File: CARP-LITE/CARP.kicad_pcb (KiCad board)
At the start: 4 copper layers, 40 x 70.1 mm, 153 parts, among them J1 USB-C, J10 PYRO_2, J11 RF_L, J3 I2C1+3V3, J4 2S XT30, J5 UART+5V+I2C1, J6 PYRO_1, J7 RF_H, J8 PWM1+5V1, J9 PWM2+5V1, Q5 SQ2318CES, Q6 SQ2318CES, Q7 SQ2318CES, SW1 SW_Push, SW2 SW_Push, U1 W25Q128JVSIMTR (16MB), U10 TPS62130A, U2 W25Q32RVXHJQ (2MB), U4 RP2350_60QFN, U5 LSM6DSO, U6 BMP390, U7 TLV75733PDBV, U9 LR2021IMLTRT, Y1 ABM8-272-T3, Y2 TG2520SMN-32.0000M-MCGNNM0

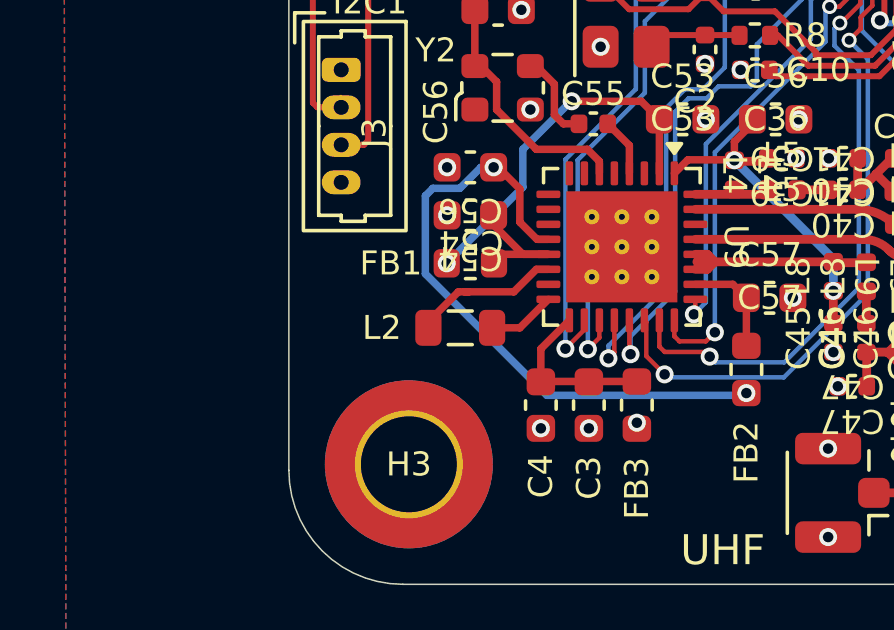
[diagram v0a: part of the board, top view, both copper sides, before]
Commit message: update inductor
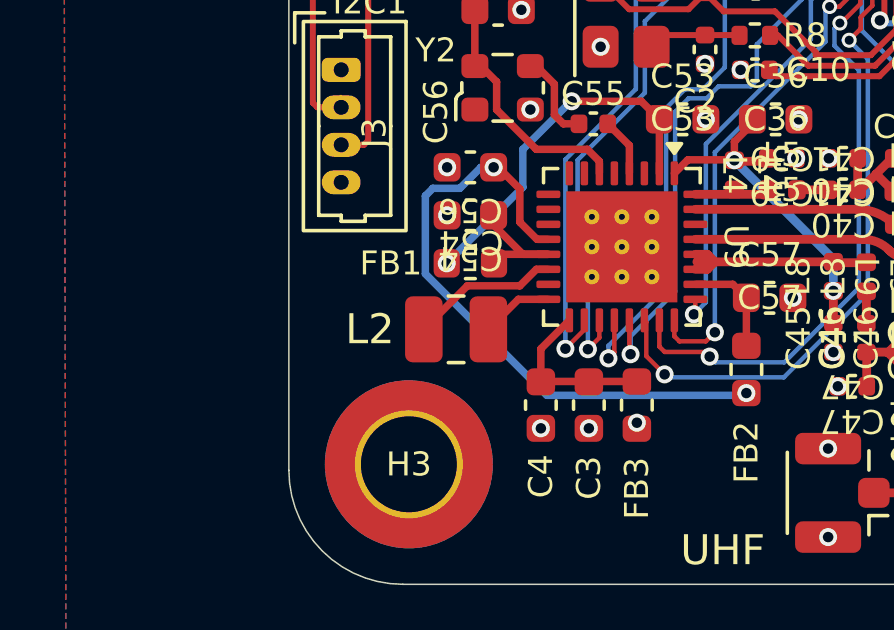
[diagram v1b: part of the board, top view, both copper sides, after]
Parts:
- L2: footprint Inductor_SMD:L_0805_2012Metric -> Inductor_SMD:L_1008_2520Metric
- moved L2 0.15 mm to (418.6, 313.3)
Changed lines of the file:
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@@
 		)
 	)
-	(footprint "Inductor_SMD:L_0805_2012Metric"
+	(footprint "Inductor_SMD:L_1008_2520Metric"
 		(layer "F.Cu")
-		(at 418.7125 313.25 180)
-		(descr "Inductor SMD 0805 (2012 Metric), square (rectangular) end terminal, IPC-7351 nominal, (Body size source: IPC-SM-782 page 80, https://www.pcb-3d.com/wordpress/wp-content/uploads/ipc-sm-782a_amendment_1_and_2.pdf)")
+		(at 418.575 313.3 180)
+		(descr "Inductor SMD 1008 (2520 Metric), square (rectangular) end terminal, IPC-7351 nominal, (Body size source: https://ecsxtal.com/store/pdf/ECS-MPI2520-SMD-POWER-INDUCTOR.pdf)")
 		(tags "inductor")
 		(property "Reference" "L2"
-			(at 2.6125 0 0)
-			(unlocked yes)
+			(at 2.875 0 0)
 			(layer "F.SilkS")
 			(effects
 				(font
-					(face "KiCad Font")
-					(size 0.8 0.8)
+					(size 1 1)
 					(thickness 0.15)
 				)
@@
 		)
 		(property "Value" "4.7u"
-			(at 0 1.55 0)
+			(at 0 2.05 0)
 			(layer "F.Fab")
 			(effects
@@
 			)
 		)
-		(property "MFR" "IMC2220ER4R7K"
+		(property "KiLib_Generator" "SMD_2terminal_chip_molded"
+			(at 0 0 0)
+			(layer "F.SilkS")
+			(hide yes)
+			(effects
+				(font
+					(size 1 1)
+					(thickness 0.15)
+				)
+			)
+		)
+		(property "MFR" "1008AF-472XJRC"
 			(at 0 0 180)
 			(unlocked yes)
@@
 		(duplicate_pad_numbers_are_jumpers no)
 		(fp_line
-			(start -0.399622 0.56)
-			(end 0.399622 0.56)
+			(start -0.261252 1.11)
+			(end 0.261252 1.11)
 			(stroke
 				(width 0.12)
@@
 		)
 		(fp_line
-			(start -0.399622 -0.56)
-			(end 0.399622 -0.56)
+			(start -0.261252 -1.11)
+			(end 0.261252 -1.11)
 			(stroke
 				(width 0.12)
@@
 		)
 		(fp_rect
-			(start -1.75 -0.85)
-			(end 1.75 0.85)
+			(start -1.95 -1.35)
+			(end 1.95 1.35)
 			(stroke
 				(width 0.05)
@@
 		)
 		(fp_rect
-			(start -1 -0.45)
-			(end 1 0.45)
+			(start -1.25 -1)
+			(end 1.25 1)
 			(stroke
 				(width 0.1)
@@
 			(layer "F.Fab")
 		)
+		(fp_text user "${REFERENCE}"
+			(at 0 0 0)
+			(layer "F.Fab")
+			(effects
+				(font
+					(size 0.62 0.62)
+					(thickness 0.09)
+				)
+			)
+		)
 		(pad "1" smd roundrect
-			(at -1.0625 0 180)
-			(size 0.875 1.2)
+			(at -1.075 0 180)
+			(size 1.25 2.2)
 			(layers "F.Cu" "F.Mask" "F.Paste")
-			(roundrect_rratio 0.25)
+			(roundrect_rratio 0.2)
 			(net "Net-(U9-LXA)")
 			(pintype "passive")
 		)
 		(pad "2" smd roundrect
-			(at 1.0625 0 180)
-			(size 0.875 1.2)
+			(at 1.075 0 180)
+			(size 1.25 2.2)
 			(layers "F.Cu" "F.Mask" "F.Paste")
-			(roundrect_rratio 0.25)
+			(roundrect_rratio 0.2)
 			(net "Net-(U9-LXB)")
 			(pintype "passive")
 		)
 		(embedded_fonts no)
-		(model "${KICAD10_3DMODEL_DIR}/Inductor_SMD.3dshapes/L_0805_2012Metric.step"
+		(model "${KICAD10_3DMODEL_DIR}/Inductor_SMD.3dshapes/L_1008_2520Metric.step"
 			(offset
 				(xyz 0 0 0)
@@
 	)
 	(segment
-		(start 419.775 313.25)
-		(end 420.7 313.25)
-		(width 0.25)
-		(layer "F.Cu")
-		(net "Net-(U9-LXA)")
-	)
-	(segment
-		(start 420.7 313.25)
+		(start 420.65 312.3)
 		(end 421.65 312.3)
 		(width 0.25)
@@
 	)
 	(segment
-		(start 421.250001 311.3)
-		(end 421.65 311.3)
+		(start 419.65 313.3)
+		(end 420.65 312.3)
 		(width 0.25)
 		(layer "F.Cu")
-		(net "Net-(U9-LXB)")
+		(net "Net-(U9-LXA)")
 	)
 	(segment
-		(start 417.65 313.05)
-		(end 418.65 312.05)
+		(start 420.700001 311.85)
+		(end 421.250001 311.3)
 		(width 0.25)
 		(layer "F.Cu")
@@
 	)
 	(segment
-		(start 418.85 312.05)
-		(end 420.500001 312.05)
+		(start 417.5 313.3)
+		(end 418.95 311.85)
 		(width 0.25)
 		(layer "F.Cu")
@@
 	)
 	(segment
-		(start 420.500001 312.05)
-		(end 421.250001 311.3)
+		(start 421.250001 311.3)
+		(end 421.65 311.3)
 		(width 0.25)
 		(layer "F.Cu")
@@
 	)
 	(segment
-		(start 418.65 312.05)
-		(end 419 312.05)
+		(start 418.95 311.85)
+		(end 420.700001 311.85)
 		(width 0.25)
 		(layer "F.Cu")

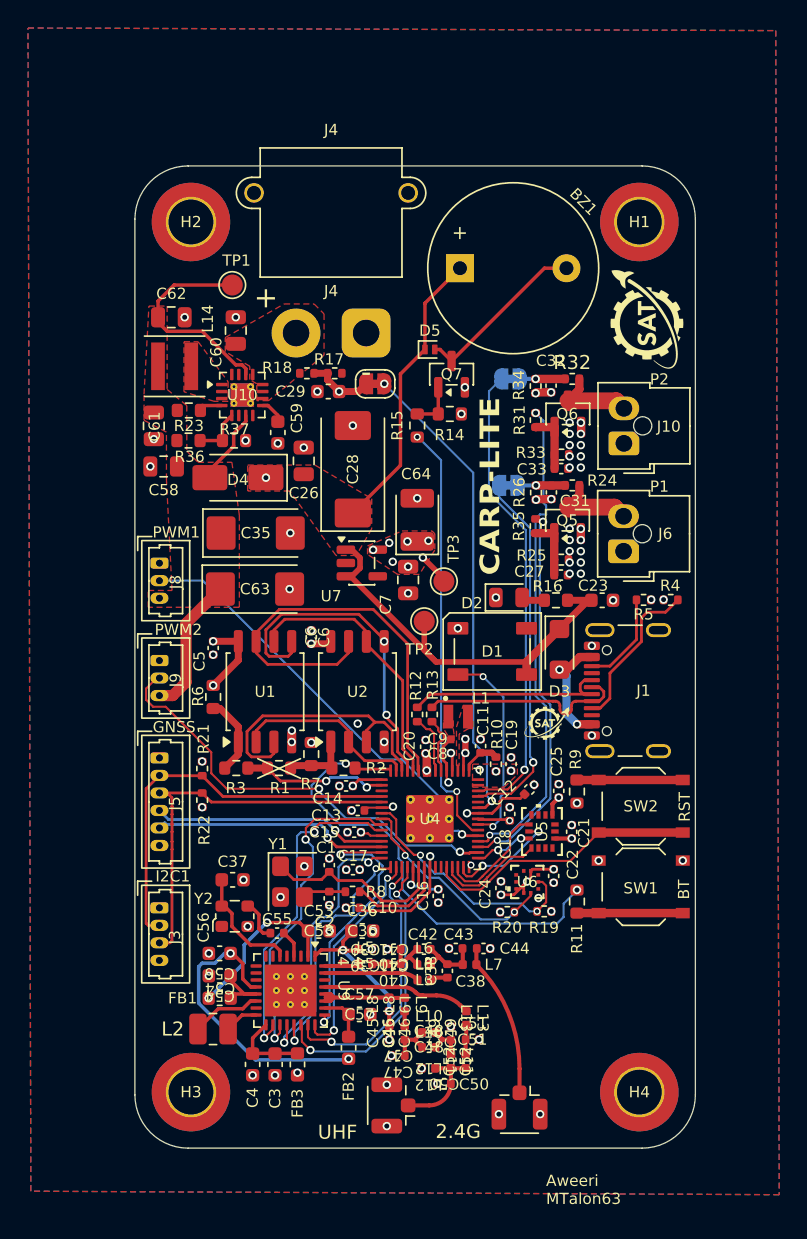
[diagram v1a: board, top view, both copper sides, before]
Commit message: radio silkscreen
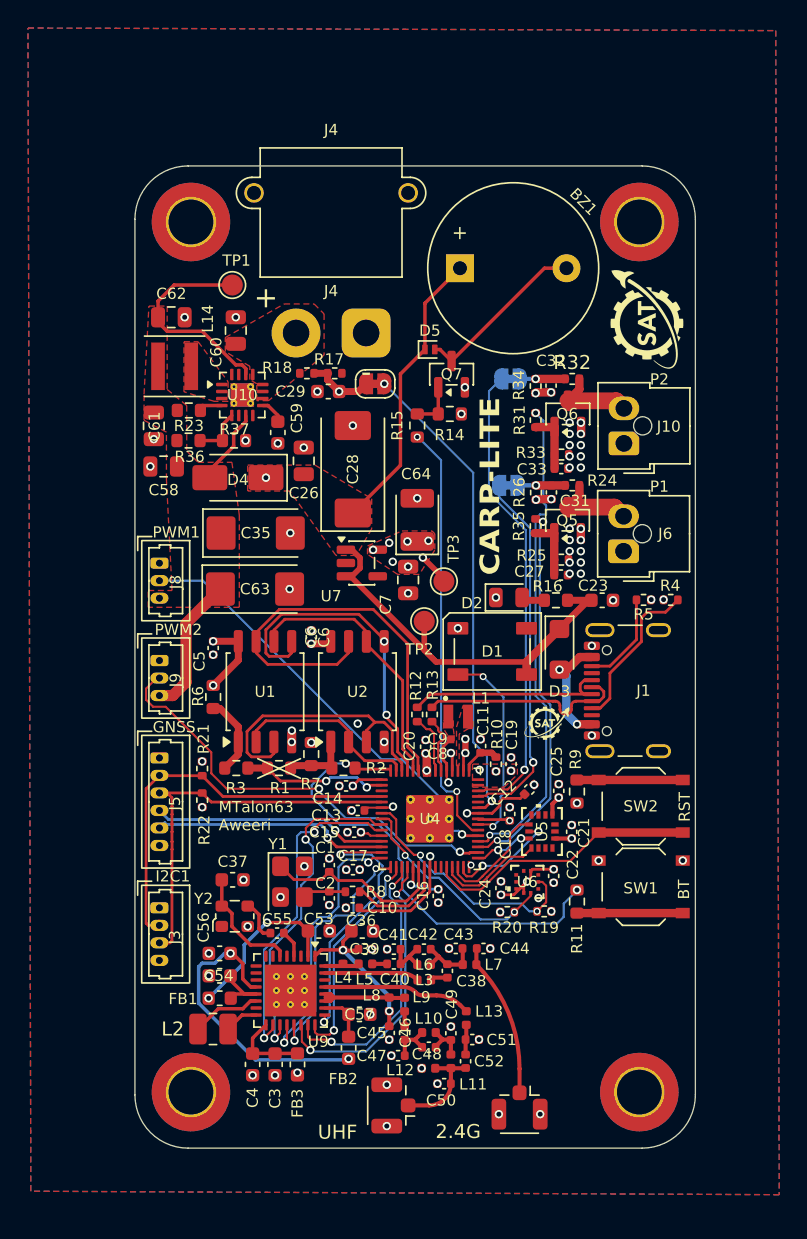
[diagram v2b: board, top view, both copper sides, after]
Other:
- board text added: "MTalon63 Aweeri"
- board text removed: "Aweeri MTalon63"

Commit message: change sizes
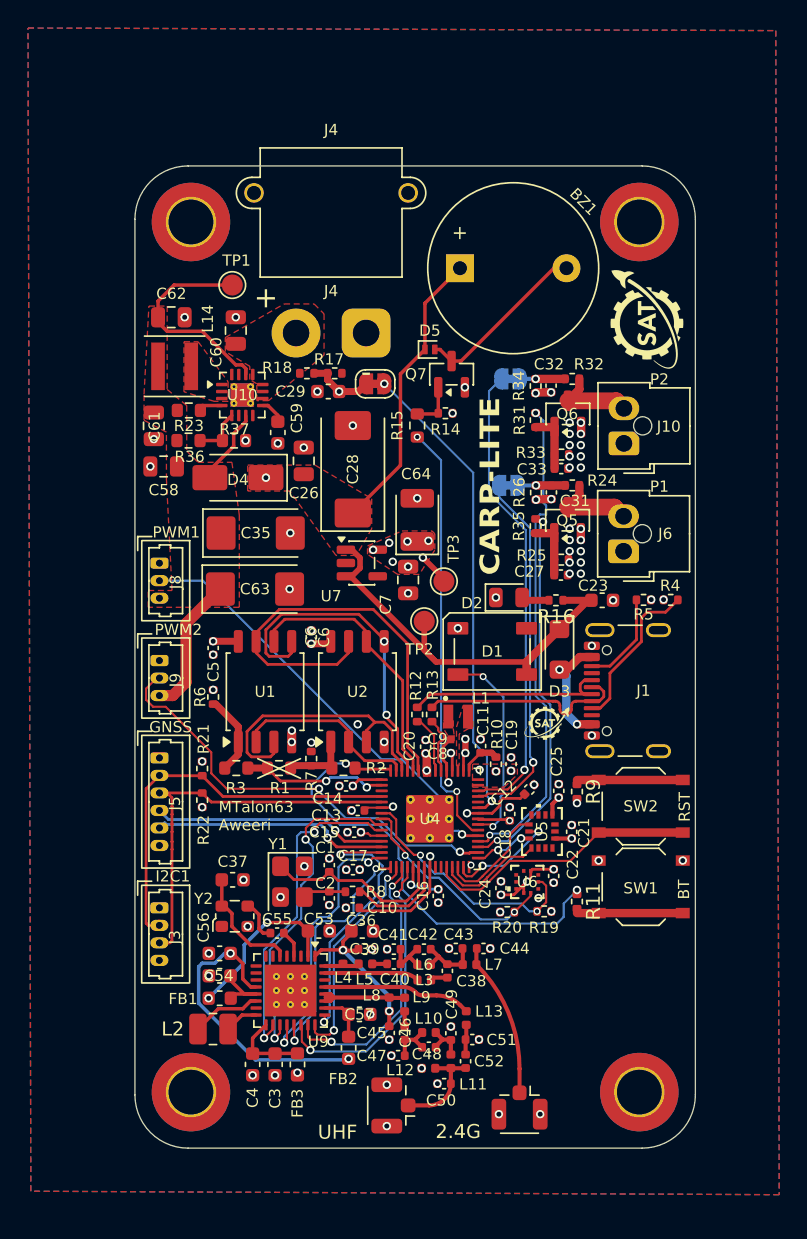
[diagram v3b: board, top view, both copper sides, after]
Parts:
- L5: value 1.5n -> 1.7n
- L7: value 1.1n -> 1n
- R11, R16, R9: footprint Resistor_SMD:R_0603_1608Metric -> Resistor_SMD:R_0402_1005Metric
- R14, R6, R7: value 10k -> 5.1k; footprint Resistor_SMD:R_0603_1608Metric -> Resistor_SMD:R_0402_1005Metric
- Y2: value TG2520SMN-32.0000M-MCGNNM0 -> ECS-TXO-25CSMV-320-AN-TR
- moved R7 0.33 mm to (425.6, 294.0)
- moved R14 0.32 mm to (435.2, 269.4)
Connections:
- R16 pad 1: +5V -> Net-(D2-A)
- R16 pad 2: Net-(D2-A) -> +5V
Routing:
- net +3V3: track 31.7 -> 27.8 mm

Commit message: change more sizes
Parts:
- R23: footprint Resistor_SMD:R_0603_1608Metric -> Resistor_SMD:R_0402_1005Metric
- moved R23 0.39 mm to (417.1, 268.9)
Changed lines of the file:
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@@
 		)
 		(fp_text user "${REFERENCE}"
-			(at 0.05 -0.05 90)
+			(at -0.85 -1.35 90)
 			(unlocked yes)
 			(layer "F.SilkS")
@@
 		)
 	)
-	(footprint "Resistor_SMD:R_0603_1608Metric"
+	(footprint "Resistor_SMD:R_0402_1005Metric"
 		(layer "F.Cu")
-		(at 416.85 269.15)
-		(descr "Resistor SMD 0603 (1608 Metric), square (rectangular) end terminal, IPC-7351 nominal, (Body size source: IPC-SM-782 page 72, https://www.pcb-3d.com/wordpress/wp-content/uploads/ipc-sm-782a_amendment_1_and_2.pdf)")
+		(at 417.15 268.9)
+		(descr "Resistor SMD 0402 (1005 Metric), square (rectangular) end terminal, IPC-7351 nominal, (Body size source: IPC-SM-782 page 72, https://www.pcb-3d.com/wordpress/wp-content/uploads/ipc-sm-782a_amendment_1_and_2.pdf)")
 		(tags "resistor")
 		(property "Reference" "R23"
-			(at 0.025 3.5 0)
-			(unlocked yes)
+			(at 0.45 1.1 0)
 			(layer "F.SilkS")
-			(hide yes)
 			(effects
 				(font
-					(face "KiCad Font")
 					(size 0.8 0.8)
 					(thickness 0.15)
@@
 		)
 		(property "Value" "100k"
-			(at 0 1.43 0)
+			(at 0 1.17 0)
 			(layer "F.Fab")
 			(effects
@@
 			)
 		)
+		(property "KiLib_Generator" "SMD_2terminal_chip_molded"
+			(at 0 0 0)
+			(layer "F.SilkS")
+			(hide yes)
+			(effects
+				(font
+					(size 1 1)
+					(thickness 0.15)
+				)
+			)
+		)
 		(property ki_fp_filters "R_*")
 		(sheetname "/")
@@
 		(duplicate_pad_numbers_are_jumpers no)
 		(fp_line
-			(start -0.237258 -0.5225)
-			(end 0.237258 -0.5225)
+			(start -0.153641 -0.38)
+			(end 0.153641 -0.38)
 			(stroke
 				(width 0.12)
@@
 		)
 		(fp_line
-			(start -0.237258 0.5225)
-			(end 0.237258 0.5225)
+			(start -0.153641 0.38)
+			(end 0.153641 0.38)
 			(stroke
 				(width 0.12)
@@
 		)
 		(fp_rect
-			(start -1.48 -0.73)
-			(end 1.48 0.73)
+			(start -0.93 -0.47)
+			(end 0.93 0.47)
 			(stroke
 				(width 0.05)
@@
 		)
 		(fp_rect
-			(start -0.8 -0.4125)
-			(end 0.8 0.4125)
+			(start -0.525 -0.27)
+			(end 0.525 0.27)
 			(stroke
 				(width 0.1)
@@
 		)
 		(fp_text user "${REFERENCE}"
-			(at 0 1.1 0)
-			(unlocked yes)
-			(layer "F.SilkS")
+			(at 0 0 0)
+			(layer "F.Fab")
 			(effects
 				(font
-					(face "KiCad Font")
-					(size 0.8 0.8)
-					(thickness 0.15)
+					(size 0.26 0.26)
+					(thickness 0.04)
 				)
 			)
 		)
 		(pad "1" smd roundrect
-			(at -0.825 0)
-			(size 0.8 0.95)
+			(at -0.51 0)
+			(size 0.54 0.64)
 			(layers "F.Cu" "F.Mask" "F.Paste")
 			(roundrect_rratio 0.25)
@@
 		)
 		(pad "2" smd roundrect
-			(at 0.825 0)
-			(size 0.8 0.95)
+			(at 0.51 0)
+			(size 0.54 0.64)
 			(layers "F.Cu" "F.Mask" "F.Paste")
 			(roundrect_rratio 0.25)
@@
 		)
 		(embedded_fonts no)
-		(model "${KICAD10_3DMODEL_DIR}/Resistor_SMD.3dshapes/R_0603_1608Metric.step"
+		(model "${KICAD10_3DMODEL_DIR}/Resistor_SMD.3dshapes/R_0402_1005Metric.step"
 			(offset
 				(xyz 0 0 0)
@@
 		)
 		(fp_text user "${REFERENCE}"
-			(at 0.075 1.15 0)
+			(at 0.225 1.15 0)
 			(unlocked yes)
 			(layer "F.SilkS")
@@
 	)
 	(segment
-		(start 417.625 268.975)
-		(end 417.625 269.15)
+		(start 419.2 268.8)
+		(end 417.8 268.8)
 		(width 0.25)
 		(layer "F.Cu")
@@
 	)
 	(segment
-		(start 417.8 268.8)
-		(end 417.625 268.975)
+		(start 417.7 268.9)
+		(end 417.66 268.9)
 		(width 0.25)
 		(layer "F.Cu")
@@
 	)
 	(segment
-		(start 419.2 268.8)
-		(end 417.8 268.8)
+		(start 417.8 268.8)
+		(end 417.7 268.9)
 		(width 0.25)
 		(layer "F.Cu")

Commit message: more sizer changers
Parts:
- R15: footprint Resistor_SMD:R_0603_1608Metric -> Resistor_SMD:R_0402_1005Metric
- moved R15 0.33 mm to (433.1, 269.9)
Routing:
- net /GPIO24: track 30.6 -> 31.2 mm
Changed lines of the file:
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@@
 		)
 		(fp_text user "${REFERENCE}"
-			(at 1.75 1.6 90)
+			(at 2.45 0.95 0)
 			(unlocked yes)
 			(layer "F.SilkS")
@@
 		)
 		(fp_text user "${REFERENCE}"
-			(at 0 0 90)
+			(at 3.35 3.1 90)
 			(unlocked yes)
 			(layer "F.SilkS")
@@
 		)
 	)
-	(footprint "Resistor_SMD:R_0603_1608Metric"
+	(footprint "Resistor_SMD:R_0402_1005Metric"
 		(layer "F.Cu")
-		(at 433.15 270.225 90)
-		(descr "Resistor SMD 0603 (1608 Metric), square (rectangular) end terminal, IPC-7351 nominal, (Body size source: IPC-SM-782 page 72, https://www.pcb-3d.com/wordpress/wp-content/uploads/ipc-sm-782a_amendment_1_and_2.pdf)")
+		(at 433.15 269.9 90)
+		(descr "Resistor SMD 0402 (1005 Metric), square (rectangular) end terminal, IPC-7351 nominal, (Body size source: IPC-SM-782 page 72, https://www.pcb-3d.com/wordpress/wp-content/uploads/ipc-sm-782a_amendment_1_and_2.pdf)")
 		(tags "resistor")
 		(property "Reference" "R15"
-			(at 0 -1.43 90)
-			(unlocked yes)
+			(at -1.65 0 180)
 			(layer "F.SilkS")
 			(effects
 				(font
-					(face "KiCad Font")
 					(size 0.8 0.8)
 					(thickness 0.15)
@@
 		)
 		(property "Value" "100"
-			(at 0 1.43 90)
+			(at 0 1.17 90)
 			(layer "F.Fab")
 			(effects
@@
 			)
 		)
+		(property "KiLib_Generator" "SMD_2terminal_chip_molded"
+			(at 0 0 90)
+			(layer "F.SilkS")
+			(hide yes)
+			(effects
+				(font
+					(size 1 1)
+					(thickness 0.15)
+				)
+			)
+		)
 		(property ki_fp_filters "R_*")
 		(sheetname "/")
@@
 		(duplicate_pad_numbers_are_jumpers no)
 		(fp_line
-			(start -0.237258 -0.5225)
-			(end 0.237258 -0.5225)
+			(start -0.153641 -0.38)
+			(end 0.153641 -0.38)
 			(stroke
 				(width 0.12)
@@
 		)
 		(fp_line
-			(start -0.237258 0.5225)
-			(end 0.237258 0.5225)
+			(start -0.153641 0.38)
+			(end 0.153641 0.38)
 			(stroke
 				(width 0.12)
@@
 		)
 		(fp_rect
-			(start -1.48 -0.73)
-			(end 1.48 0.73)
+			(start -0.93 -0.47)
+			(end 0.93 0.47)
 			(stroke
 				(width 0.05)
@@
 		)
 		(fp_rect
-			(start -0.8 -0.4125)
-			(end 0.8 0.4125)
+			(start -0.525 -0.27)
+			(end 0.525 0.27)
 			(stroke
 				(width 0.1)
@@
 			(layer "F.Fab")
 		)
+		(fp_text user "${REFERENCE}"
+			(at 0 0 90)
+			(layer "F.Fab")
+			(effects
+				(font
+					(size 0.26 0.26)
+					(thickness 0.04)
+				)
+			)
+		)
 		(pad "1" smd roundrect
-			(at -0.825 0 90)
-			(size 0.8 0.95)
+			(at -0.51 0 90)
+			(size 0.54 0.64)
 			(layers "F.Cu" "F.Mask" "F.Paste")
 			(roundrect_rratio 0.25)
@@
 		)
 		(pad "2" smd roundrect
-			(at 0.825 0 90)
-			(size 0.8 0.95)
+			(at 0.51 0 90)
+			(size 0.54 0.64)
 			(layers "F.Cu" "F.Mask" "F.Paste")
 			(roundrect_rratio 0.25)
@@
 		)
 		(embedded_fonts no)
-		(model "${KICAD10_3DMODEL_DIR}/Resistor_SMD.3dshapes/R_0603_1608Metric.step"
+		(model "${KICAD10_3DMODEL_DIR}/Resistor_SMD.3dshapes/R_0402_1005Metric.step"
 			(offset
 				(xyz 0 0 0)
@@
 		)
 		(fp_text user "${REFERENCE}"
-			(at 0 0 0)
+			(at 4.43 0 90)
 			(unlocked yes)
 			(layer "F.SilkS")
@@
 		)
 		(fp_text user "${REFERENCE}"
-			(at 0 0 0)
+			(at 4.38 1.05 90)
 			(unlocked yes)
 			(layer "F.SilkS")
@@
 		)
 		(fp_text user "${REFERENCE}"
-			(at -2.19328 2.361315 0)
+			(at 0.95672 2.411315 0)
 			(unlocked yes)
 			(layer "F.SilkS")
@@
 		(tags "resistor")
 		(property "Reference" "R14"
-			(at 0 1.15 0)
+			(at 0 1.1 0)
 			(layer "F.SilkS")
 			(effects
@@
 	)
 	(via
-		(at 433.15 271.05)
+		(at 433.15 270.41)
 		(size 0.5)
 		(drill 0.3)
@@
 	)
 	(segment
-		(start 435.242939 296.342939)
-		(end 434.85 295.95)
-		(width 0.15)
-		(layer "B.Cu")
-		(net "/GPIO24")
-	)
-	(segment
-		(start 433.2 271.05)
-		(end 433.15 271.05)
+		(start 434.85 295.95)
+		(end 435.242939 296.342939)
 		(width 0.15)
 		(layer "B.Cu")
@@
 	)
 	(segment
-		(start 434.85 295.95)
-		(end 434.85 272.7)
+		(start 433.15 270.41)
+		(end 434.85 272.11)
 		(width 0.15)
 		(layer "B.Cu")
@@
 	)
 	(segment
-		(start 434.85 272.7)
-		(end 433.2 271.05)
+		(start 435.972161 296.342939)
+		(end 435.92299 296.293768)
 		(width 0.15)
 		(layer "B.Cu")
@@
 	)
 	(segment
-		(start 435.972161 296.342939)
-		(end 435.92299 296.293768)
+		(start 435.242939 296.342939)
+		(end 435.972161 296.342939)
 		(width 0.15)
 		(layer "B.Cu")
@@
 	)
 	(segment
-		(start 435.972161 296.342939)
-		(end 435.242939 296.342939)
+		(start 434.85 272.11)
+		(end 434.85 295.95)
 		(width 0.15)
 		(layer "B.Cu")
